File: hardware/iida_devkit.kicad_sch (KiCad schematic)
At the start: 7 parts

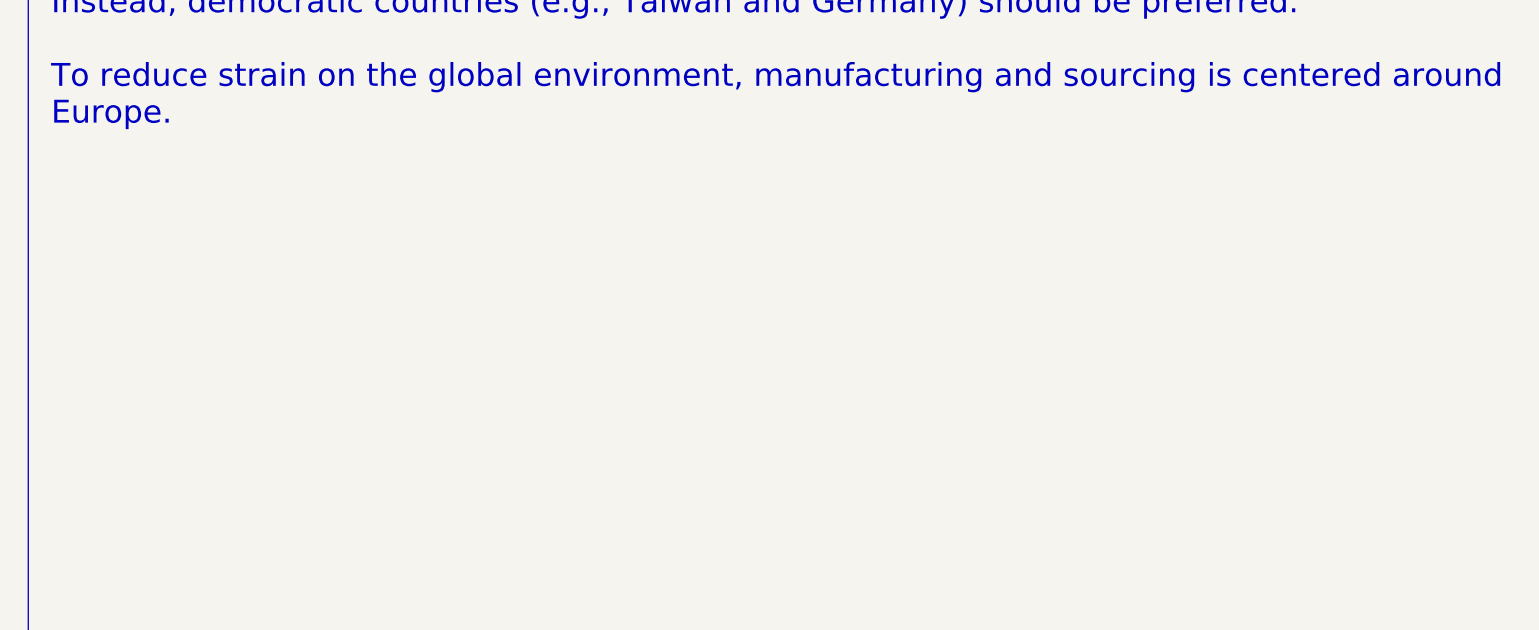
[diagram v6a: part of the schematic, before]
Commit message: HW: Unused GPIOs to headers, refine schematics
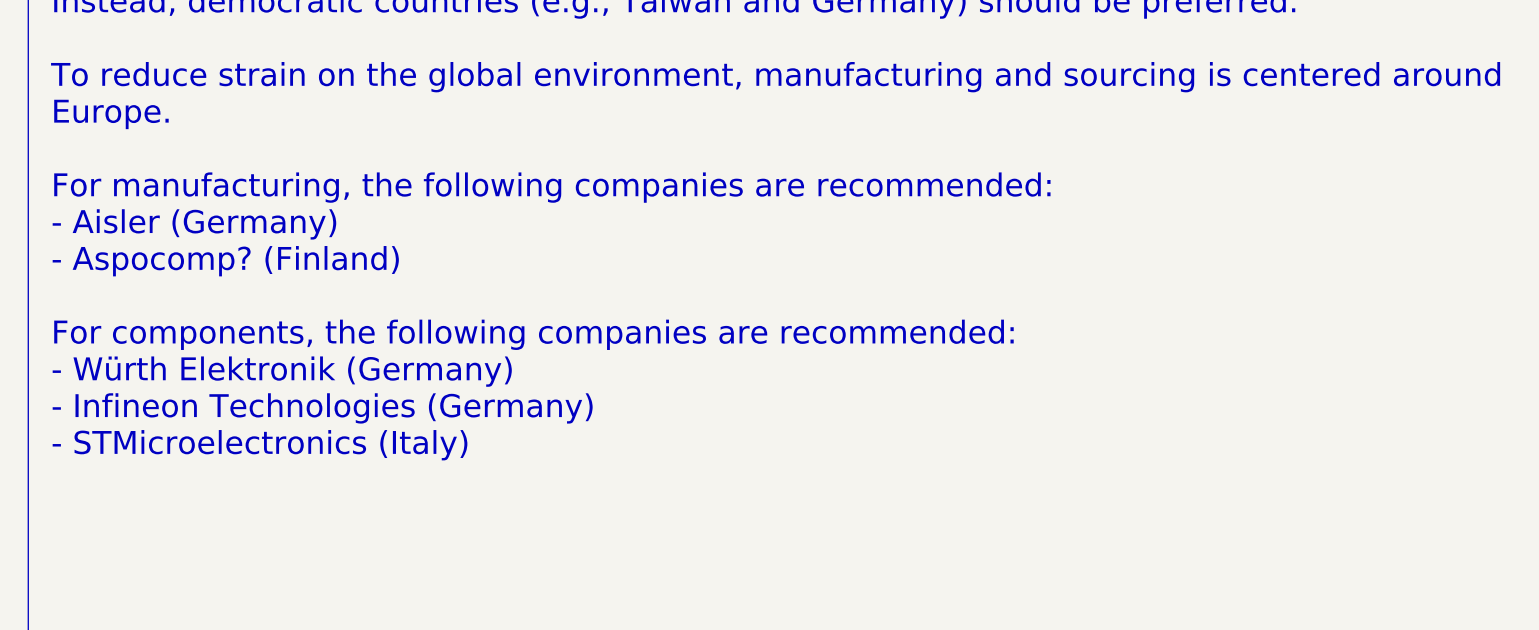
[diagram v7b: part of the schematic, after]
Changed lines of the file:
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@@
 	(title_block
 		(title "Iida devkit")
-		(date "2025-05-08")
+		(date "2025-05-09")
 		(rev "v5.0.0")
 	)
@@
 		)
 	)
-	(text "This is a project for practicing PCB design and programming.\n\nThe result is a device that is powered either with a battery or with a USB connection.\nThe device can recharge the battery via the USB connection.\n\nThe device includes:\n  - An example sensor (temperature)\n  - External flash for updating the firmware over the air (FOTA)\n  - A modem module that connects the main microcontroller to the internet with LTE CAT-M1\n  - Option to use either an external antenna or an integrated antenna\n\nA key goal of the project is to ensure it has as little reliance as possible on totalitarian\ncountries (e.g., China or Russia) or on hostile countries (e.g., USA).\nComponent sourcing must be done carefully to select manufacturers who can supply parts\nthat are not produced in such countries.\nInstead, democratic countries (e.g., Taiwan and Germany) should be preferred.\n\nTo reduce strain on the global environment, manufacturing and sourcing is centered around\nEurope."
+	(text "This is a project for practicing PCB design and programming.\n\nThe result is a device that is powered either with a battery or with a USB connection.\nThe device can recharge the battery via the USB connection.\n\nThe device includes:\n  - An example sensor (temperature)\n  - External flash for updating the firmware over the air (FOTA)\n  - A modem module that connects the main microcontroller to the internet with LTE CAT-M1\n  - Option to use either an external antenna or an integrated antenna\n\nA key goal of the project is to ensure it has as little reliance as possible on totalitarian\ncountries (e.g., China or Russia) or on hostile countries (e.g., USA).\nComponent sourcing must be done carefully to select manufacturers who can supply parts\nthat are not produced in such countries.\nInstead, democratic countries (e.g., Taiwan and Germany) should be preferred.\n\nTo reduce strain on the global environment, manufacturing and sourcing is centered around\nEurope.\n\nFor manufacturing, the following companies are recommended:\n- Aisler (Germany)\n- Aspocomp? (Finland)\n\nFor components, the following companies are recommended:\n- Würth Elektronik (Germany)\n- Infineon Technologies (Germany)\n- STMicroelectronics (Italy)"
 		(exclude_from_sim no)
 		(at 15.24 63.5 0)
@@
 			)
 		)
+		(property "Manufacturer Part Number" ""
+			(at 39.37 274.32 0)
+			(effects
+				(font
+					(size 1.27 1.27)
+				)
+				(hide yes)
+			)
+		)
 		(pin "1"
 		)
@@
 		)
 		(property "Power" ""
+			(at 54.61 274.32 0)
+			(effects
+				(font
+					(size 1.27 1.27)
+				)
+				(hide yes)
+			)
+		)
+		(property "Manufacturer Part Number" ""
 			(at 54.61 274.32 0)
 			(effects
@@
 			)
 		)
+		(property "Manufacturer Part Number" ""
+			(at 114.3 273.05 0)
+			(effects
+				(font
+					(size 1.27 1.27)
+				)
+				(hide yes)
+			)
+		)
 		(instances
 			(project "iida_devkit"
@@
 			)
 		)
+		(property "Manufacturer Part Number" ""
+			(at 44.45 274.32 0)
+			(effects
+				(font
+					(size 1.27 1.27)
+				)
+				(hide yes)
+			)
+		)
 		(pin "1"
 		)
@@
 			)
 		)
+		(property "Manufacturer Part Number" ""
+			(at 101.6 273.05 0)
+			(effects
+				(font
+					(size 1.27 1.27)
+				)
+				(hide yes)
+			)
+		)
 		(instances
 			(project ""
@@
 			)
 		)
+		(property "Manufacturer Part Number" ""
+			(at 127 273.05 0)
+			(effects
+				(font
+					(size 1.27 1.27)
+				)
+				(hide yes)
+			)
+		)
 		(instances
 			(project "iida_devkit"
@@
 			(at 49.53 274.32 0)
 			(effects
+				(font
+					(size 1.27 1.27)
+				)
+				(hide yes)
+			)
+		)
+		(property "Manufacturer Part Number" ""
+			(at 49.53 274.32 0)
+			(effects

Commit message: HW: Refine BOM, add comments, color code power rails
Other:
- note added: "- Layout comments are in magenta"
- note added: "- Mechanical comments are in green"
- note added: "- Schematic comments are in blue"
- note added: "Place a stitched GND guard rail around the edges of the PCB to provide a grounding point for human touch when handling the device."
- note added: "Place fiducials at three corners of the PCB."
- note removed: "Place a stitched GND guard rail around the edges of the PCB to provide a grounding point for human touch."
- note removed: "Place fiducials on three corners of the PCB."
- moved on the sheet: FID1, FID2, FID3, H1, H2, H3, H4
